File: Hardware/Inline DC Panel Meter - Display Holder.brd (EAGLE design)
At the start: 63.5 x 38.1 mm, 7 parts

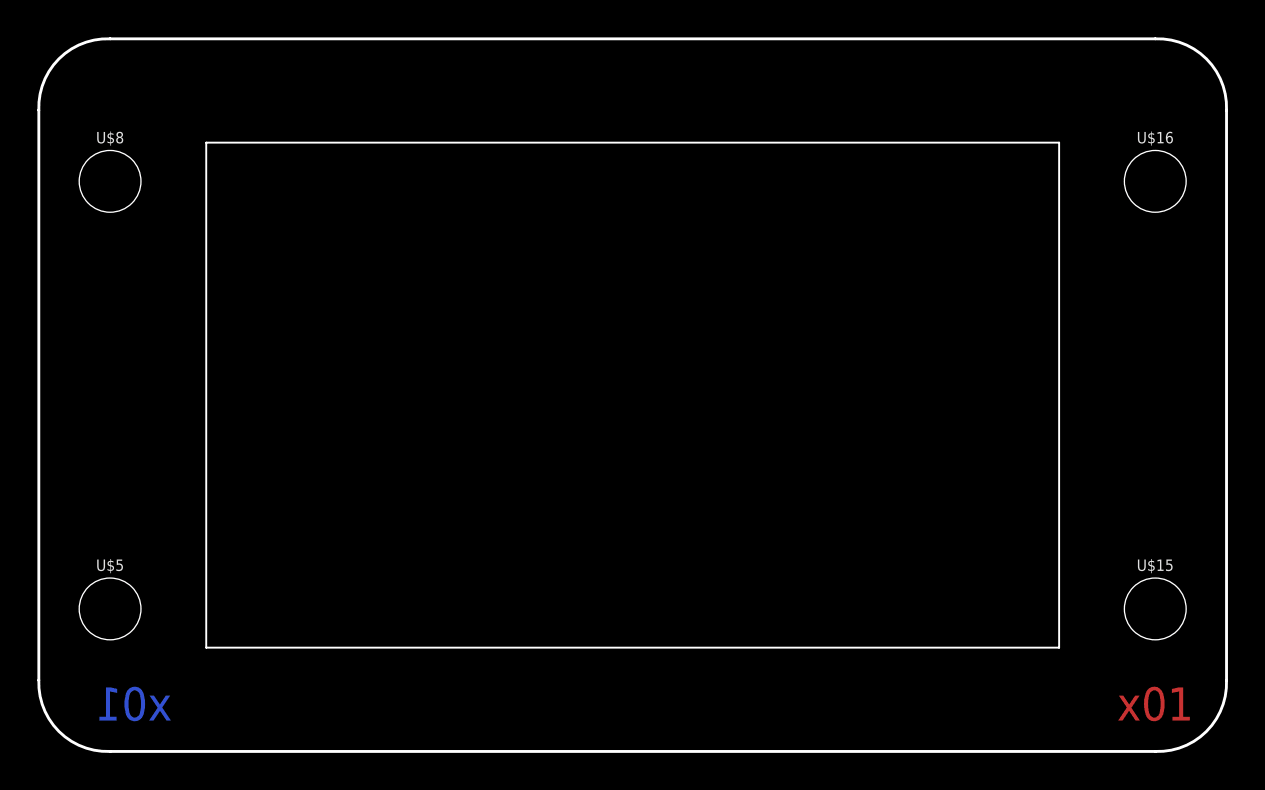
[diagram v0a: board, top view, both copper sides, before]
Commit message: Decrease window size for x02.
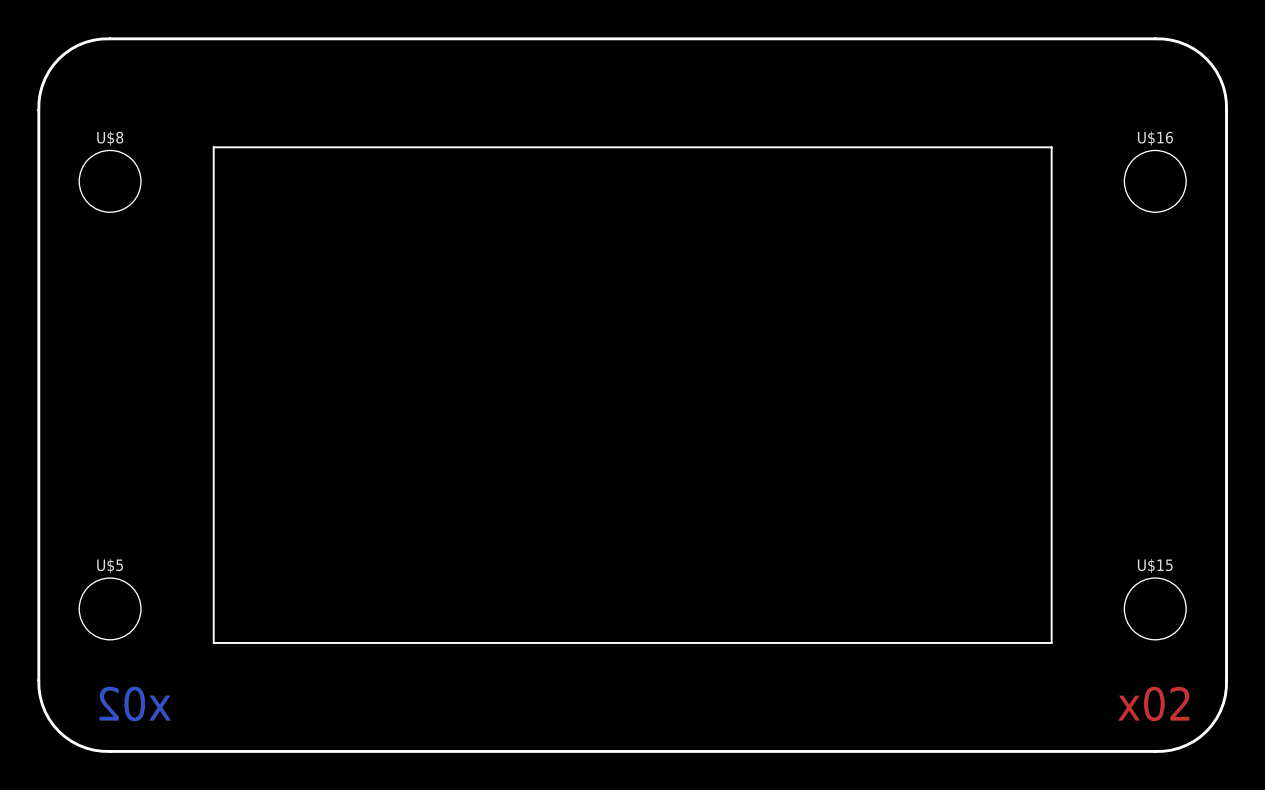
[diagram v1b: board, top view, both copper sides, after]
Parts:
- removed U$6: (no value), LFP-Battery-Bridge:METER
- added U$2: (no value), Panel Mount Meter:METER
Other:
- board text added: "x02"
- board text removed: "x01"
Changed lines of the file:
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@@
 <layer number="23" name="tOrigins" color="15" fill="1" visible="yes" active="yes"/>
 <layer number="24" name="bOrigins" color="15" fill="1" visible="yes" active="yes"/>
-<layer number="25" name="tNames" color="7" fill="1" visible="yes" active="yes"/>
-<layer number="26" name="bNames" color="7" fill="1" visible="yes" active="yes"/>
-<layer number="27" name="tValues" color="7" fill="1" visible="yes" active="yes"/>
-<layer number="28" name="bValues" color="7" fill="1" visible="yes" active="yes"/>
-<layer number="29" name="tStop" color="7" fill="6" visible="yes" active="yes"/>
-<layer number="30" name="bStop" color="7" fill="3" visible="yes" active="yes"/>
-<layer number="31" name="tCream" color="7" fill="5" visible="yes" active="yes"/>
-<layer number="32" name="bCream" color="7" fill="4" visible="yes" active="yes"/>
-<layer number="33" name="tFinish" color="6" fill="3" visible="yes" active="yes"/>
-<layer number="34" name="bFinish" color="6" fill="6" visible="yes" active="yes"/>
-<layer number="35" name="tGlue" color="7" fill="4" visible="yes" active="yes"/>
-<layer number="36" name="bGlue" color="7" fill="5" visible="yes" active="yes"/>
-<layer number="37" name="tTest" color="7" fill="1" visible="yes" active="yes"/>
-<layer number="38" name="bTest" color="7" fill="1" visible="yes" active="yes"/>
-<layer number="39" name="tKeepout" color="4" fill="11" visible="yes" active="yes"/>
-<layer number="40" name="bKeepout" color="1" fill="11" visible="yes" active="yes"/>
-<layer number="41" name="tRestrict" color="4" fill="10" visible="yes" active="yes"/>
-<layer number="42" name="bRestrict" color="1" fill="10" visible="yes" active="yes"/>
-<layer number="43" name="vRestrict" color="2" fill="10" visible="yes" active="yes"/>
-<layer number="44" name="Drills" color="7" fill="1" visible="yes" active="yes"/>
+<layer number="25" name="tNames" color="7" fill="1" visible="no" active="yes"/>
+<layer number="26" name="bNames" color="7" fill="1" visible="no" active="yes"/>
+<layer number="27" name="tValues" color="7" fill="1" visible="no" active="yes"/>
+<layer number="28" name="bValues" color="7" fill="1" visible="no" active="yes"/>
+<layer number="29" name="tStop" color="7" fill="6" visible="no" active="yes"/>
+<layer number="30" name="bStop" color="7" fill="3" visible="no" active="yes"/>
+<layer number="31" name="tCream" color="7" fill="5" visible="no" active="yes"/>
+<layer number="32" name="bCream" color="7" fill="4" visible="no" active="yes"/>
+<layer number="33" name="tFinish" color="6" fill="3" visible="no" active="yes"/>
+<layer number="34" name="bFinish" color="6" fill="6" visible="no" active="yes"/>
+<layer number="35" name="tGlue" color="7" fill="4" visible="no" active="yes"/>
+<layer number="36" name="bGlue" color="7" fill="5" visible="no" active="yes"/>
+<layer number="37" name="tTest" color="7" fill="1" visible="no" active="yes"/>
+<layer number="38" name="bTest" color="7" fill="1" visible="no" active="yes"/>
+<layer number="39" name="tKeepout" color="4" fill="11" visible="no" active="yes"/>
+<layer number="40" name="bKeepout" color="1" fill="11" visible="no" active="yes"/>
+<layer number="41" name="tRestrict" color="4" fill="10" visible="no" active="yes"/>
+<layer number="42" name="bRestrict" color="1" fill="10" visible="no" active="yes"/>
+<layer number="43" name="vRestrict" color="2" fill="10" visible="no" active="yes"/>
+<layer number="44" name="Drills" color="7" fill="1" visible="no" active="yes"/>
 <layer number="45" name="Holes" color="7" fill="1" visible="yes" active="yes"/>
-<layer number="46" name="Milling" color="3" fill="1" visible="yes" active="yes"/>
-<layer number="47" name="Measures" color="7" fill="1" visible="yes" active="yes"/>
-<layer number="48" name="Document" color="7" fill="1" visible="yes" active="yes"/>
-<layer number="49" name="Reference" color="7" fill="1" visible="yes" active="yes"/>
-<layer number="50" name="dxf" color="7" fill="1" visible="yes" active="yes"/>
+<layer number="46" name="Milling" color="3" fill="1" visible="no" active="yes"/>
+<layer number="47" name="Measures" color="7" fill="1" visible="no" active="yes"/>
+<layer number="48" name="Document" color="7" fill="1" visible="no" active="yes"/>
+<layer number="49" name="Reference" color="7" fill="1" visible="no" active="yes"/>
+<layer number="50" name="dxf" color="7" fill="1" visible="no" active="yes"/>
 <layer number="51" name="tDocu" color="6" fill="1" visible="yes" active="yes"/>
-<layer number="52" name="bDocu" color="6" fill="1" visible="yes" active="yes"/>
+<layer number="52" name="bDocu" color="6" fill="1" visible="no" active="yes"/>
 <layer number="2" name="Route2" color="1" fill="3" visible="no" active="no"/>
 <layer number="15" name="Route15" color="4" fill="6" visible="no" active="no"/>
@@
 <wire x1="3.81" y1="0" x2="0" y2="3.81" width="0.1524" layer="20" curve="-94.422753"/>
 <wire x1="63.5" y1="3.81" x2="59.69" y2="0" width="0.1524" layer="20" curve="-94.422753"/>
-<text x="59.69" y="2.54" size="1.778" layer="1" font="vector" ratio="15" align="center">x01</text>
-<text x="5.08" y="2.54" size="1.778" layer="16" font="vector" ratio="15" rot="MR0" align="center">x01</text>
+<text x="59.69" y="2.54" size="1.778" layer="1" font="vector" ratio="15" align="center">x02</text>
+<text x="5.08" y="2.54" size="1.778" layer="16" font="vector" ratio="15" rot="MR0" align="center">x02</text>
 </plain>
 <attributes>
@@
 <attribute name="REV" value="" x="15.24" y="-36.83" size="1.778" layer="27" font="vector" ratio="15" display="off"/>
 </element>
-<element name="U$6" library="LFP-Battery-Bridge" package="METER" value="" x="31.75" y="19.05" smashed="yes"/>
 <element name="U$8" library="SparkFun-Hardware" package="STAND-OFF" value="" x="3.81" y="30.48" smashed="yes">
 <attribute name="NAME" x="3.81" y="32.512" size="0.6096" layer="25" font="vector" ratio="20" align="bottom-center"/>
@@
 </element>
 <element name="U$1" library="SparkX" package="SPARKX-MEDIUM" value="SPARKX-LOGO4" x="31.75" y="2.54" smashed="yes" rot="MR0"/>
+<element name="U$2" library="Panel Mount Meter" package="METER" value="" x="31.75" y="19.05" smashed="yes"/>
 </elements>
 <signals>
